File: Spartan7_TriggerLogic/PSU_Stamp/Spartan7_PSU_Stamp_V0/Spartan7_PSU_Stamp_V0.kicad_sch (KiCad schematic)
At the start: 1 part, among them J1 USB4125-GF-A

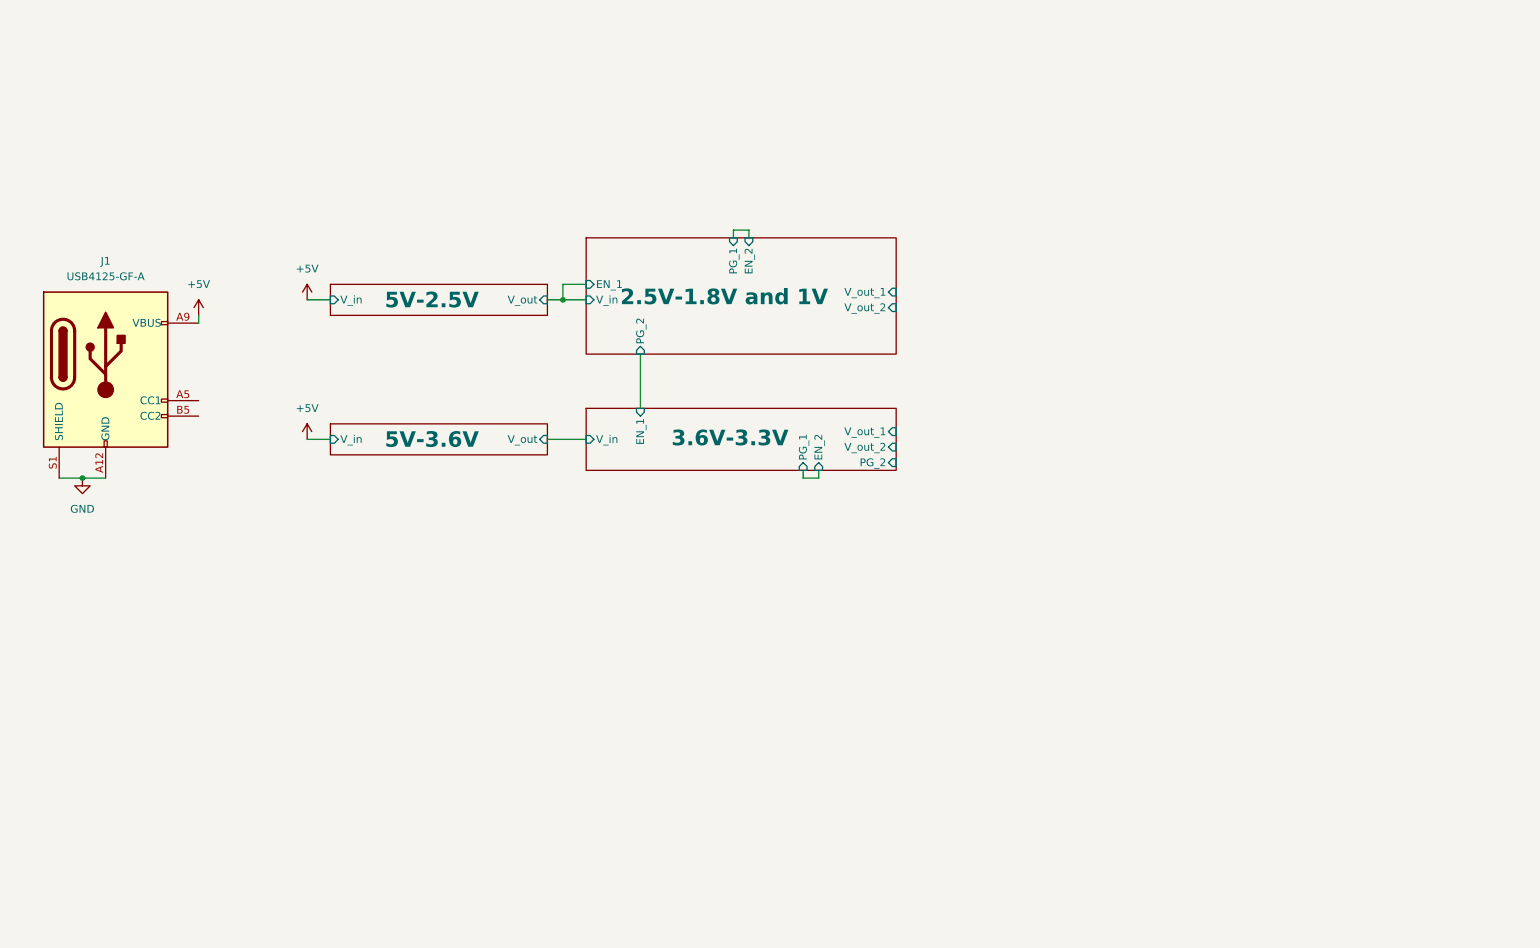
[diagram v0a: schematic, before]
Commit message: Add USB-C power and TPS7A2033PDBVR symbol
Added USB_C_Power schematic, new TPS7A2033PDBVR symbol and library, and updated net names and layout for improved clarity. Also included new backup files and made minor footprint and netlist adjustments for the Spartan7 PSU Stamp project.
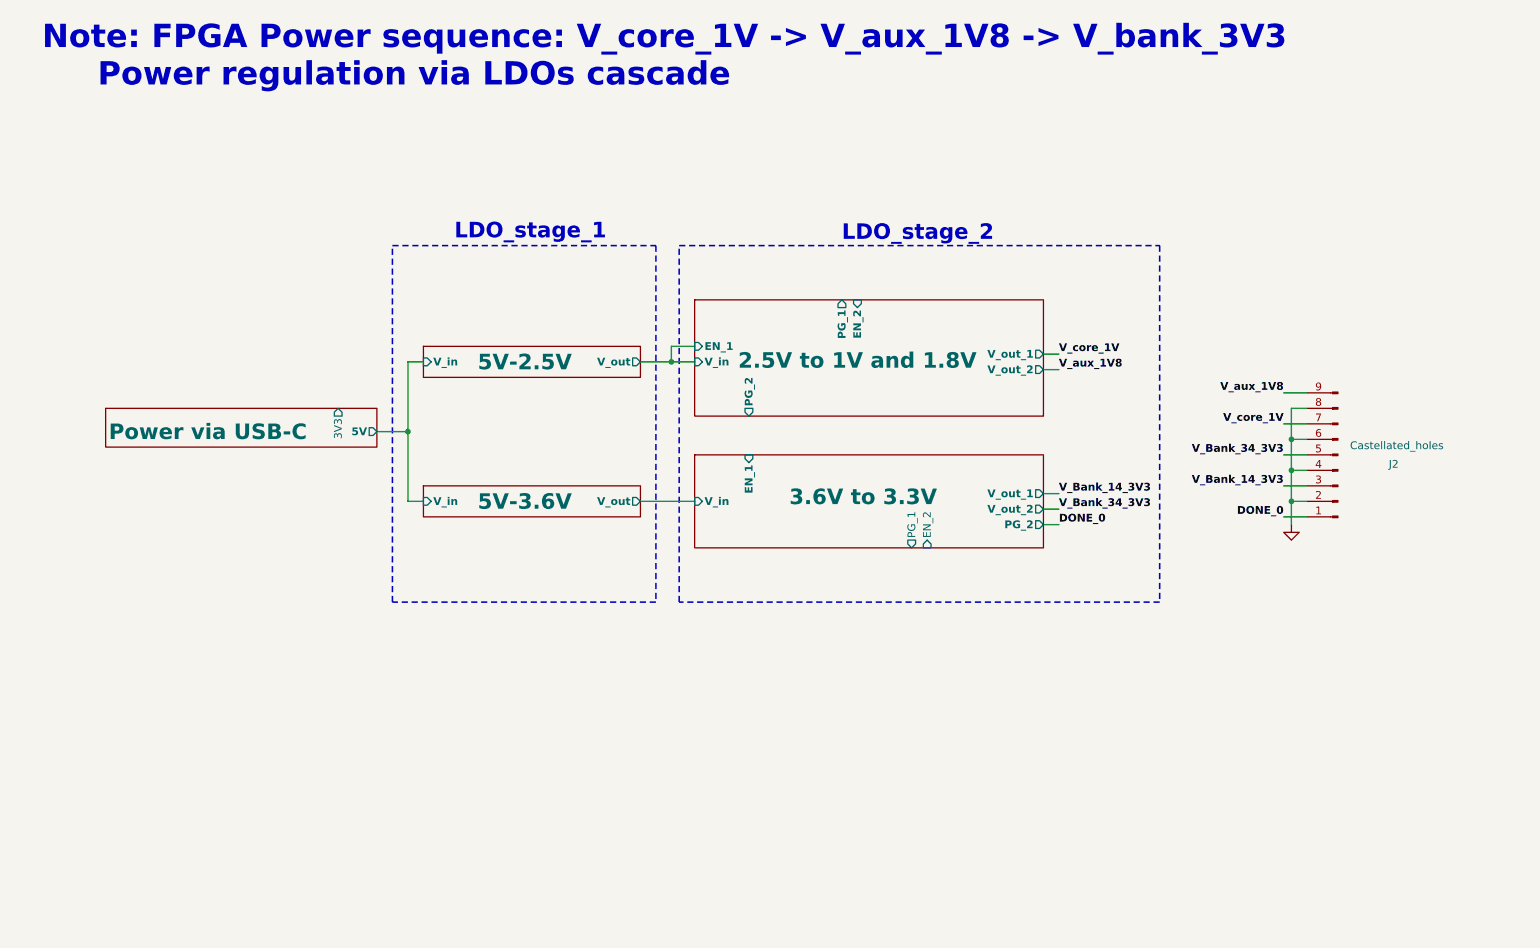
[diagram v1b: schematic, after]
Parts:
- removed J1: USB4125-GF-A, Connector_USB:USB_C_Receptacle_HRO_TYPE-C-31-M-17, symbol Connector:USB_C_Receptacle_PowerOnly_6P
- added J2: Castellated_holes, Connector_PinHeader_2.54mm:PinHeader_1x09_P2.54mm_Vertical, symbol Connector:Conn_01x09_Pin
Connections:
- net GND: now also J2.2 (Pin_2), J2.4 (Pin_4), J2.6 (Pin_6), J2.8 (Pin_8)
- new net DONE_0: J2.1 (Pin_1)
- new net V_Bank_14_3V3: J2.3 (Pin_3)
- new net V_Bank_34_3V3: J2.5 (Pin_5)
- new net V_aux_1V8: J2.9 (Pin_9)
- new net V_core_1V: J2.7 (Pin_7)
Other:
- sheet 2.5V-1.8V and 1V renamed 2.5V to 1V and 1.8V
- sheet 3.6V-3.3V renamed 3.6V to 3.3V
- added sheet Power via USB-C (USB_C_Power.kicad_sch)
- note added: "LDO_stage_1"
- note added: "LDO_stage_2"
- note added: "Note: FPGA Power sequence: V_core_1V -> V_aux_1V8 -> V_bank_3V3 Power regulation via LDOs cascade"
- title: PSU Stamp for Spartan7 -> PSU Stamp for Spartan7-FTGB196

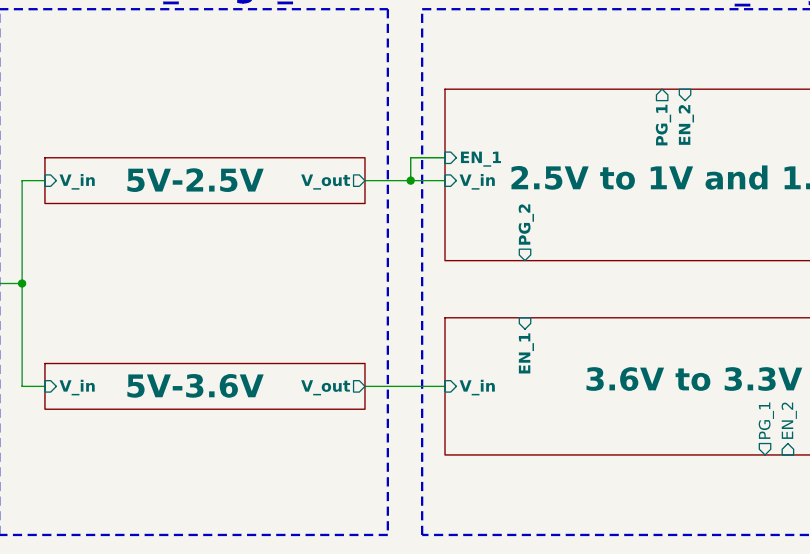
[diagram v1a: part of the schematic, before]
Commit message: Update net assignments and add vias in KiCad PCB
Reassigned several net numbers and names in Spartan7_PSU_Stamp_V0.kicad_pcb for improved clarity and consistency. Added multiple via definitions and updated related PCB segments. Removed old backup files and added new ones to the backups directory.
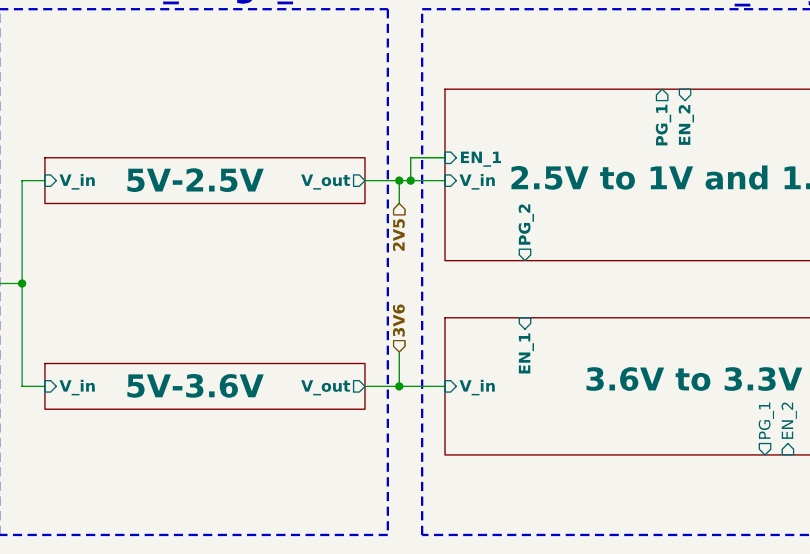
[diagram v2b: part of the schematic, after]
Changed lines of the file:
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@@
+	)
+	(junction
+		(at 146.05 111.76)
+		(diameter 0)
+		(color 0 0 0 0)
 	)
 	(junction
@@
 	)
 	(junction
+		(at 146.05 88.9)
+		(diameter 0)
+		(color 0 0 0 0)
+	)
+	(junction
 		(at 147.32 88.9)
 		(diameter 0)
@@
 	(wire
 		(pts
-			(xy 142.24 88.9) (xy 147.32 88.9)
+			(xy 142.24 88.9) (xy 146.05 88.9)
 		)
 		(stroke
@@
 	(wire
 		(pts
+			(xy 146.05 107.95) (xy 146.05 111.76)
+		)
+		(stroke
+			(width 0)
+			(type default)
+		)
+	)
+	(wire
+		(pts
 			(xy 208.28 113.03) (xy 210.82 113.03)
 		)
@@
 	(wire
 		(pts
-			(xy 142.24 111.76) (xy 151.13 111.76)
+			(xy 146.05 88.9) (xy 147.32 88.9)
+		)
+		(stroke
+			(width 0)
+			(type default)
+		)
+	)
+	(wire
+		(pts
+			(xy 142.24 111.76) (xy 146.05 111.76)
 		)
 		(stroke
@@
 	(wire
 		(pts
+			(xy 146.05 91.44) (xy 146.05 88.9)
+		)
+		(stroke
+			(width 0)
+			(type default)
+		)
+	)
+	(wire
+		(pts
 			(xy 151.13 86.36) (xy 147.32 86.36)
 		)
@@
 		(pts
 			(xy 99.06 100.33) (xy 104.14 100.33)
+		)
+		(stroke
+			(width 0)
+			(type default)
+		)
+	)
+	(wire
+		(pts
+			(xy 146.05 111.76) (xy 151.13 111.76)
 		)
 		(stroke
@@
 		)
 	)
+	(hierarchical_label "2V5"
+		(shape input)
+		(at 146.05 91.44 270)
+		(effects
+			(font
+				(size 1.27 1.27)
+				(thickness 0.254)
+				(bold yes)
+			)
+			(justify right)
+		)
+	)
+	(hierarchical_label "3V6"
+		(shape input)
+		(at 146.05 107.95 90)
+		(effects
+			(font
+				(size 1.27 1.27)
+				(thickness 0.254)
+				(bold yes)
+			)
+			(justify left)
+		)
+	)

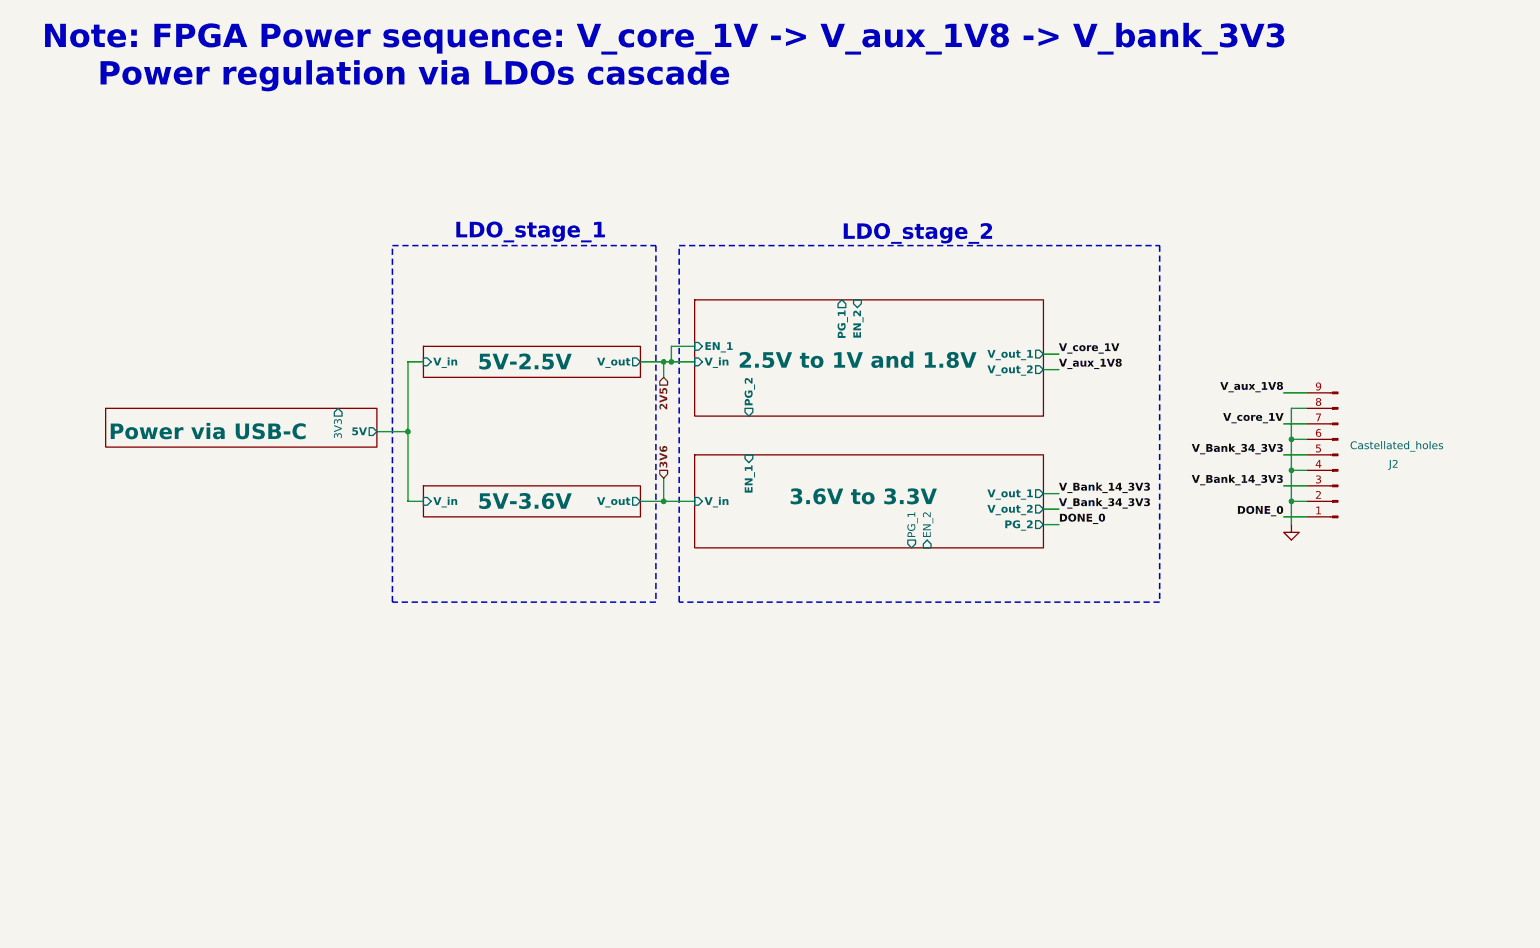
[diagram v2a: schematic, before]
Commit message: Add status LEDs and update power nets
Added new 0402 LEDs (D1, D4) and supporting resistor (R12) for power-good status indication. Updated net assignments and replaced a capacitor footprint with an LED. Modified schematic and PCB files to reflect these changes.
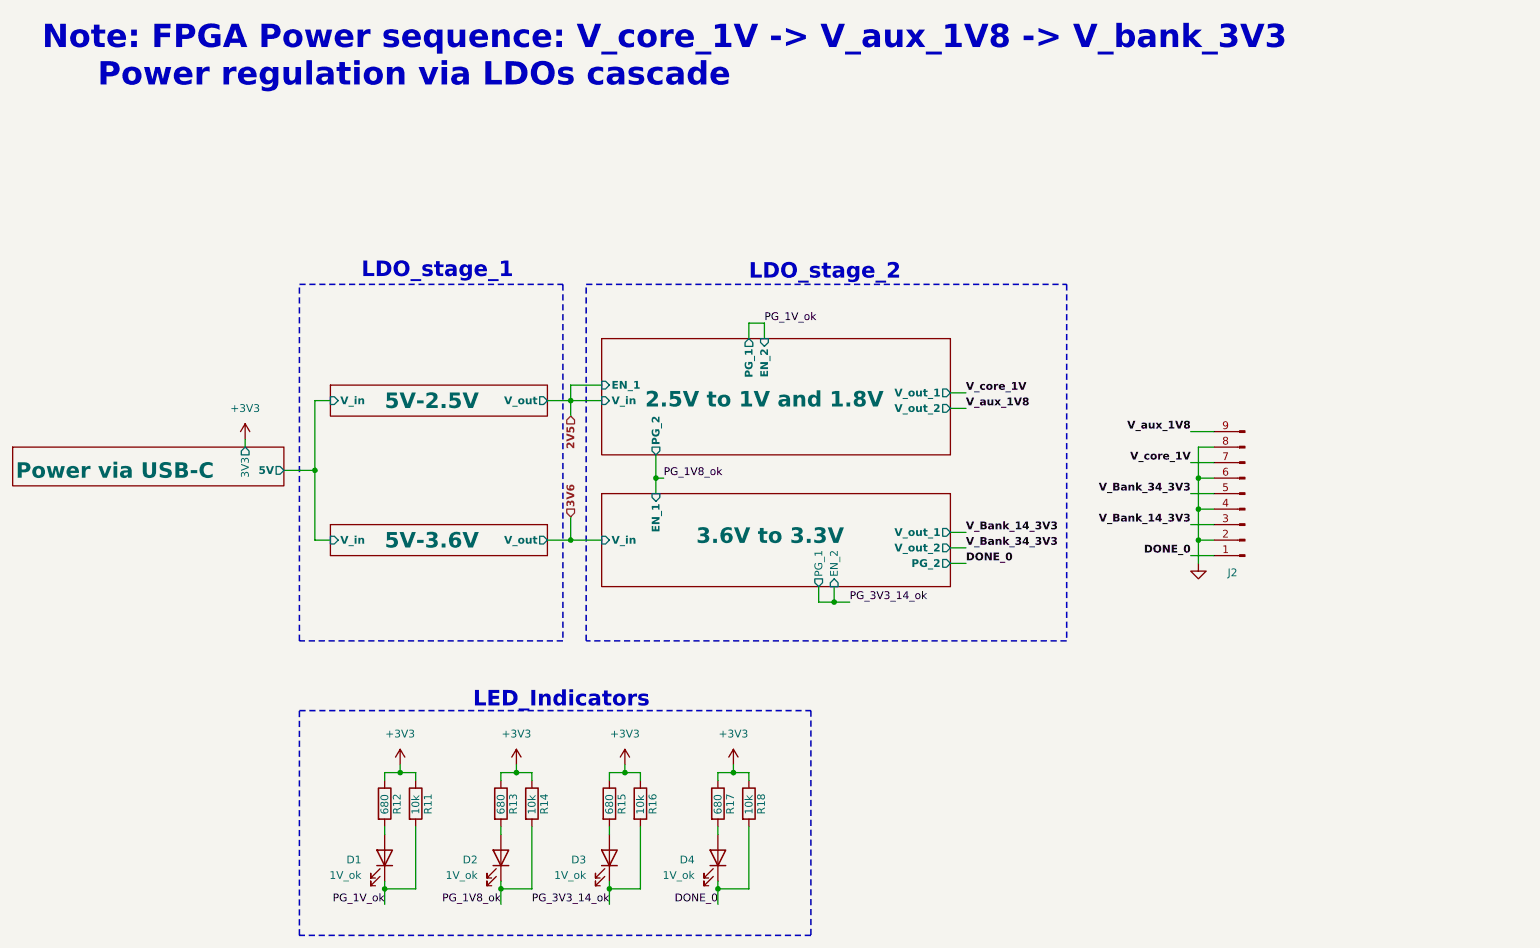
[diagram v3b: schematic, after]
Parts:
- added D1, D2, D3, D4: 1V_ok, LED_SMD:LED_0402_1005Metric, symbol Device:LED
- added R11, R14, R16, R18: 10k, Resistor_SMD:R_0402_1005Metric, symbol Device:R
- added R12, R13, R15, R17: 680, Resistor_SMD:R_0402_1005Metric, symbol Device:R
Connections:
- net DONE_0: now also D4.1 (K), R18.2
- new net: D3.2 (A), R15.2
- new net: D4.2 (A), R17.2
- new net: D2.2 (A), R13.2
- new net: D1.2 (A), R12.2
- new net +3V3: R11.1, R12.1, R13.1, R14.1, R15.1, R16.1, R17.1, R18.1
- new net PG_1V8_ok: D2.1 (K), R14.2
- new net PG_1V_ok: D1.1 (K), R11.2
- new net PG_3V3_14_ok: D3.1 (K), R16.2
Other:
- note added: "LED_Indicators"
- moved on the sheet: J2

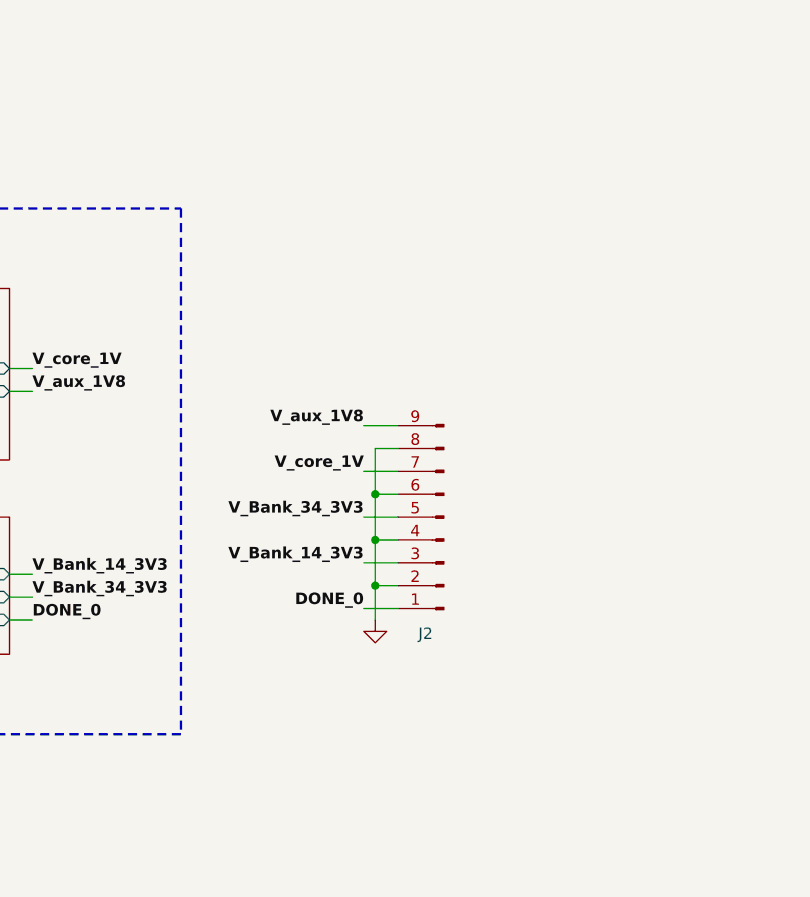
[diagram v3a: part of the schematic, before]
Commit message: Update PCB netlist and add GND test point
Renumbered and cleaned up net assignments in the KiCad PCB file, updated several resistor values, and added a new GND test point (J4). Also updated backup and plot files to reflect the latest schematic and layout changes.
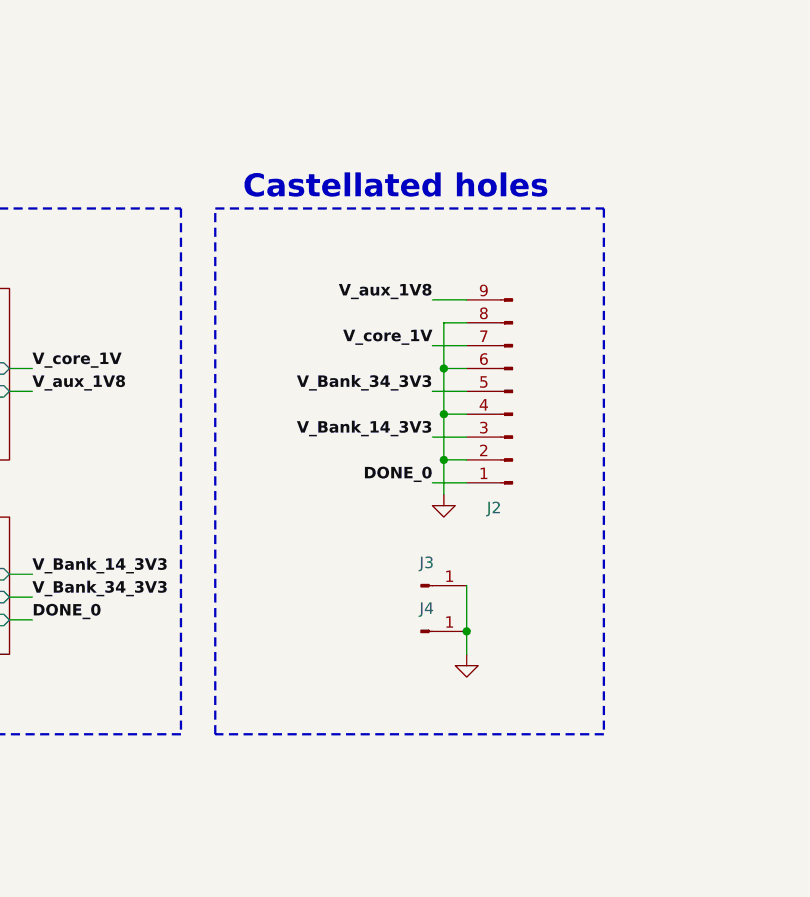
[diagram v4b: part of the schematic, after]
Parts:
- added J3, J4: Conn_01x01_Pin, symbol Connector:Conn_01x01_Pin
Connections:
- net GND: now also J3.1 (Pin_1), J4.1 (Pin_1)
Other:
- note added: "Castellated holes"
- moved on the sheet: J2
